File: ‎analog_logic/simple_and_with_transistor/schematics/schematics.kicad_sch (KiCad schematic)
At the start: 8 parts, among them Q1 BC547, Q2 BC547

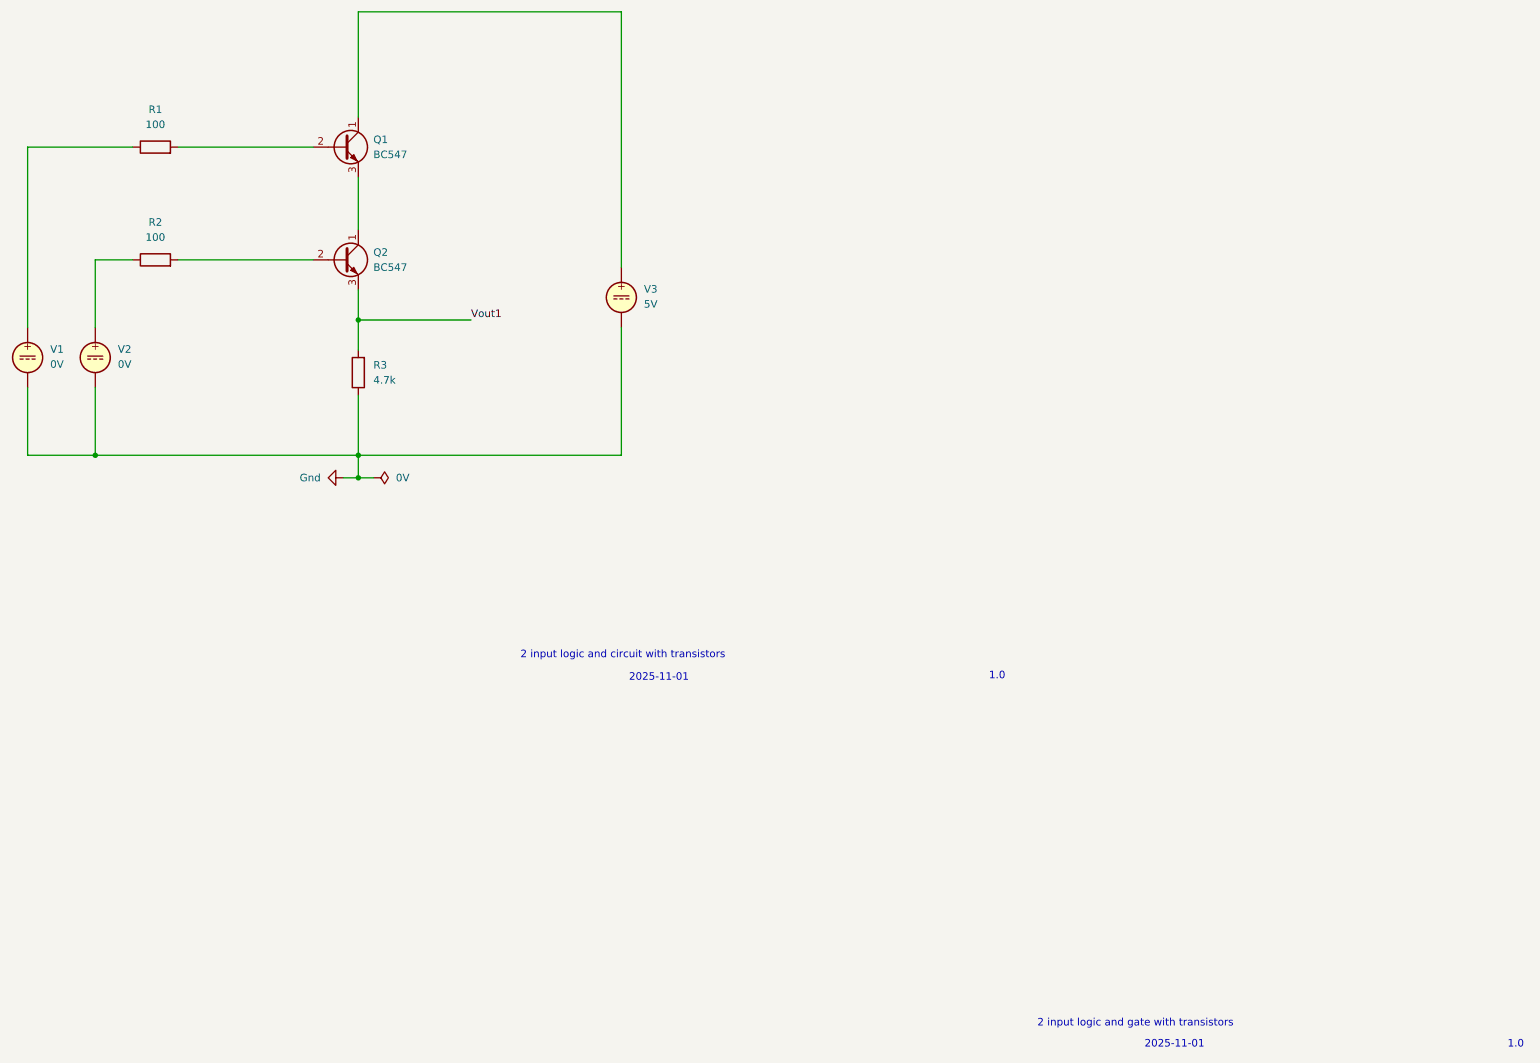
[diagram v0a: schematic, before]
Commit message: docs: Updates documentation
Changes the layout of the github pages so that they are easier to
document later.

Fixes an error on the analog_logic for AND logic gate with transistor
where the wrong schematic image was being used.

Breaking changes: None

Resolves: None
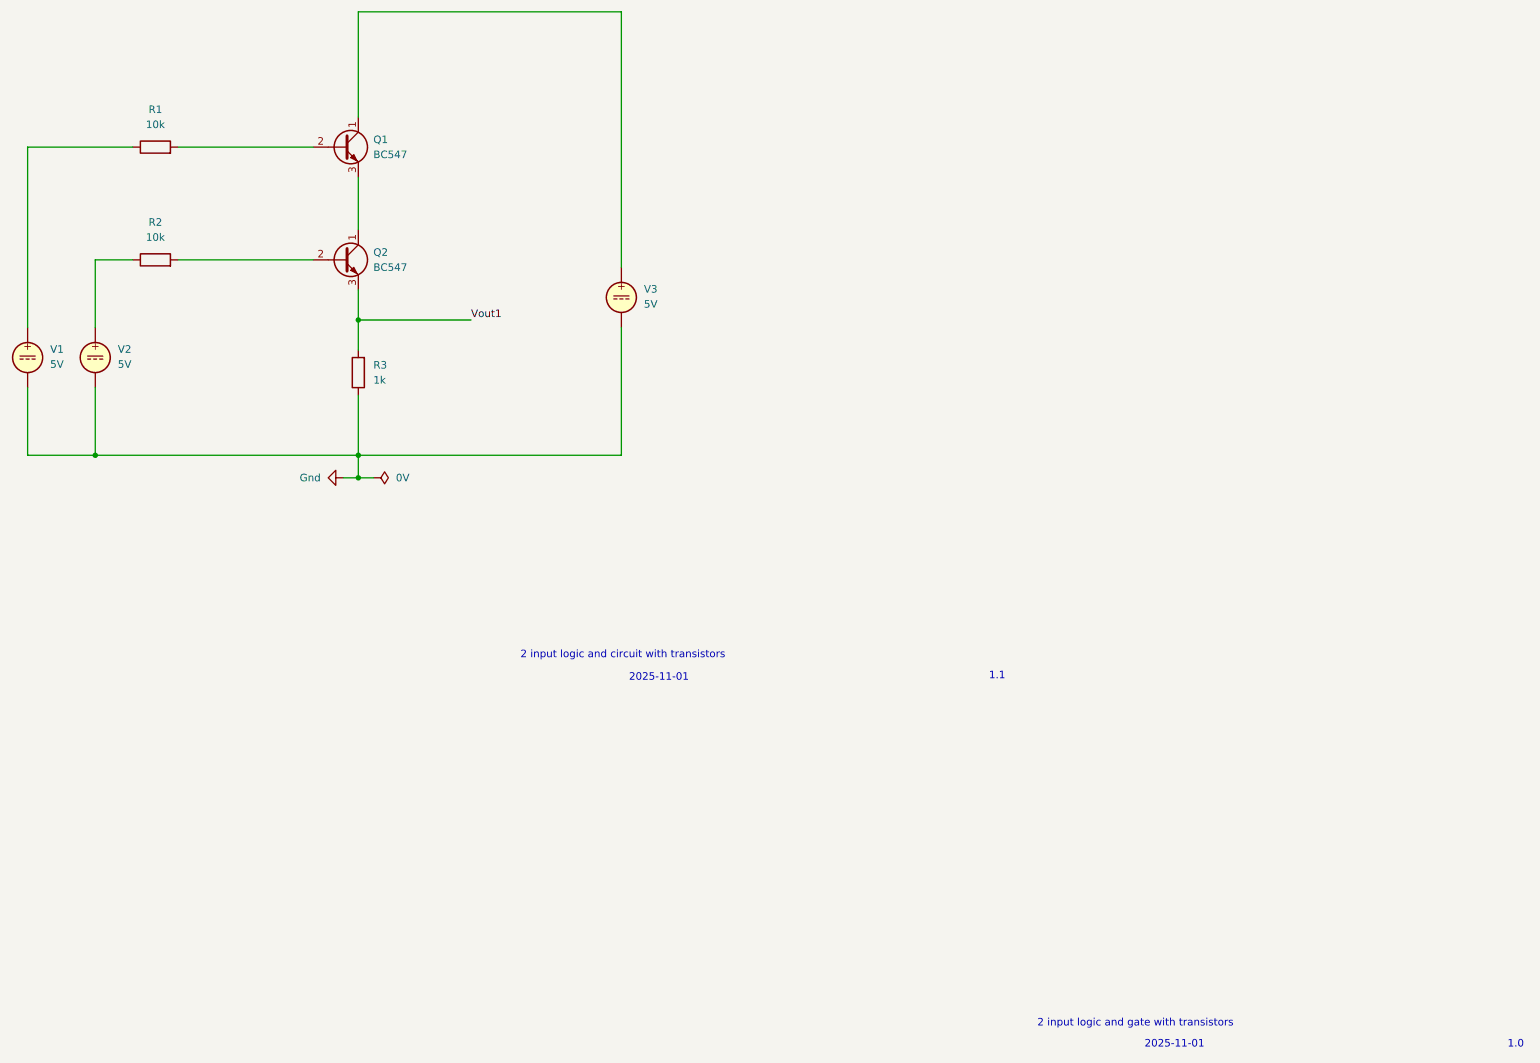
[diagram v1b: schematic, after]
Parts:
- R1, R2: value 100 -> 10k
- R3: value 4.7k -> 1k
- V1, V2: value 0V -> 5V
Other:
- note added: "1.1"
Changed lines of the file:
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@@
 		)
 	)
-	(text "1.0"
+	(text "1.1"
 		(exclude_from_sim no)
 		(at 182.88 131.318 0)
@@
 			)
 		)
-		(property "Value" "100"
+		(property "Value" "10k"
 			(at 40.64 57.15 90)
 			(effects
@@
 			)
 		)
-		(property "Value" "100"
+		(property "Value" "10k"
 			(at 40.64 38.1 90)
 			(effects
@@
 			)
 		)
-		(property "Value" "0V"
+		(property "Value" "5V"
 			(at 22.86 78.6101 0)
 			(effects
@@
 			)
 		)
-		(property "Value" "0V"
+		(property "Value" "5V"
 			(at 34.29 78.6101 0)
 			(effects
@@
 			)
 		)
-		(property "Value" "4.7k"
+		(property "Value" "1k"
 			(at 77.47 81.2799 0)
 			(effects
